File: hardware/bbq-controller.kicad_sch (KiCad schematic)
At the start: 18 parts, among them J1 Barrel_Jack, J2 Probe_Pit, J3 Probe_Meat1, J4 Probe_Meat2, J5 WT32-SC01_Plus, J6 Servo_MG90S, J7 Fan_5015, Q1 IRLZ44N, U1 MP1584EN, U2 ADS1115

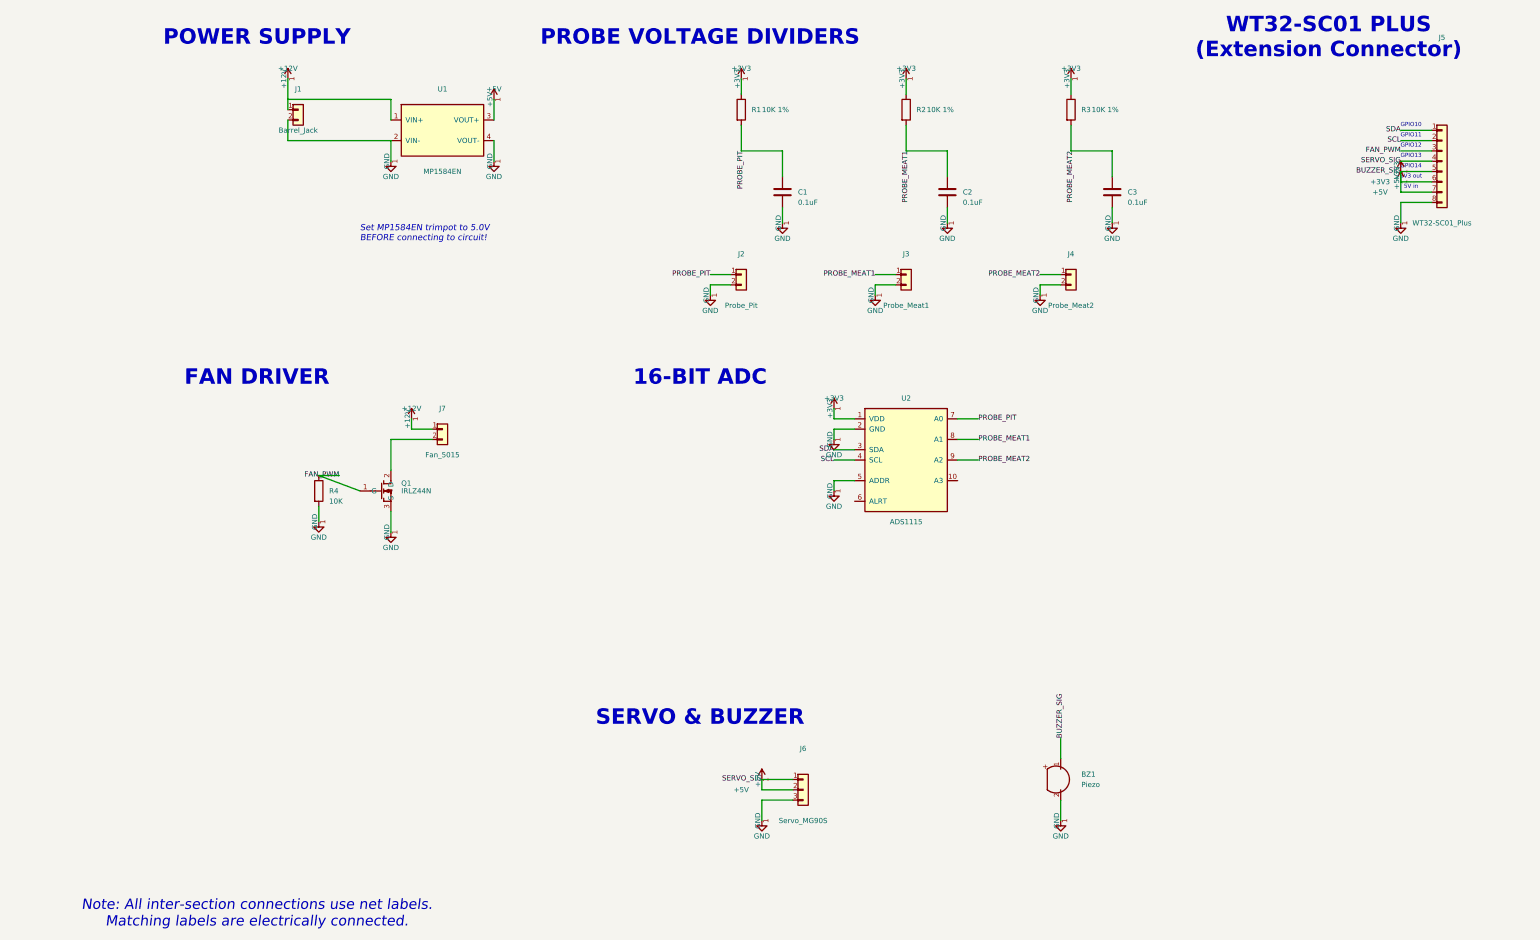
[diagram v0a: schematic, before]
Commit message: Fix KiCad schematic wiring and add perfboard layout to assembly guide
Rewrote the KiCad schematic using a Python generator script that computes
exact pin-to-wire coordinates, fixing all disconnected components. Added a
detailed perfboard layout section to the assembly guide showing component
placement on the 50x70mm board with grid references and back-side wiring
instructions.

Co-Authored-By: Claude Opus 4.6 <noreply@anthropic.com>
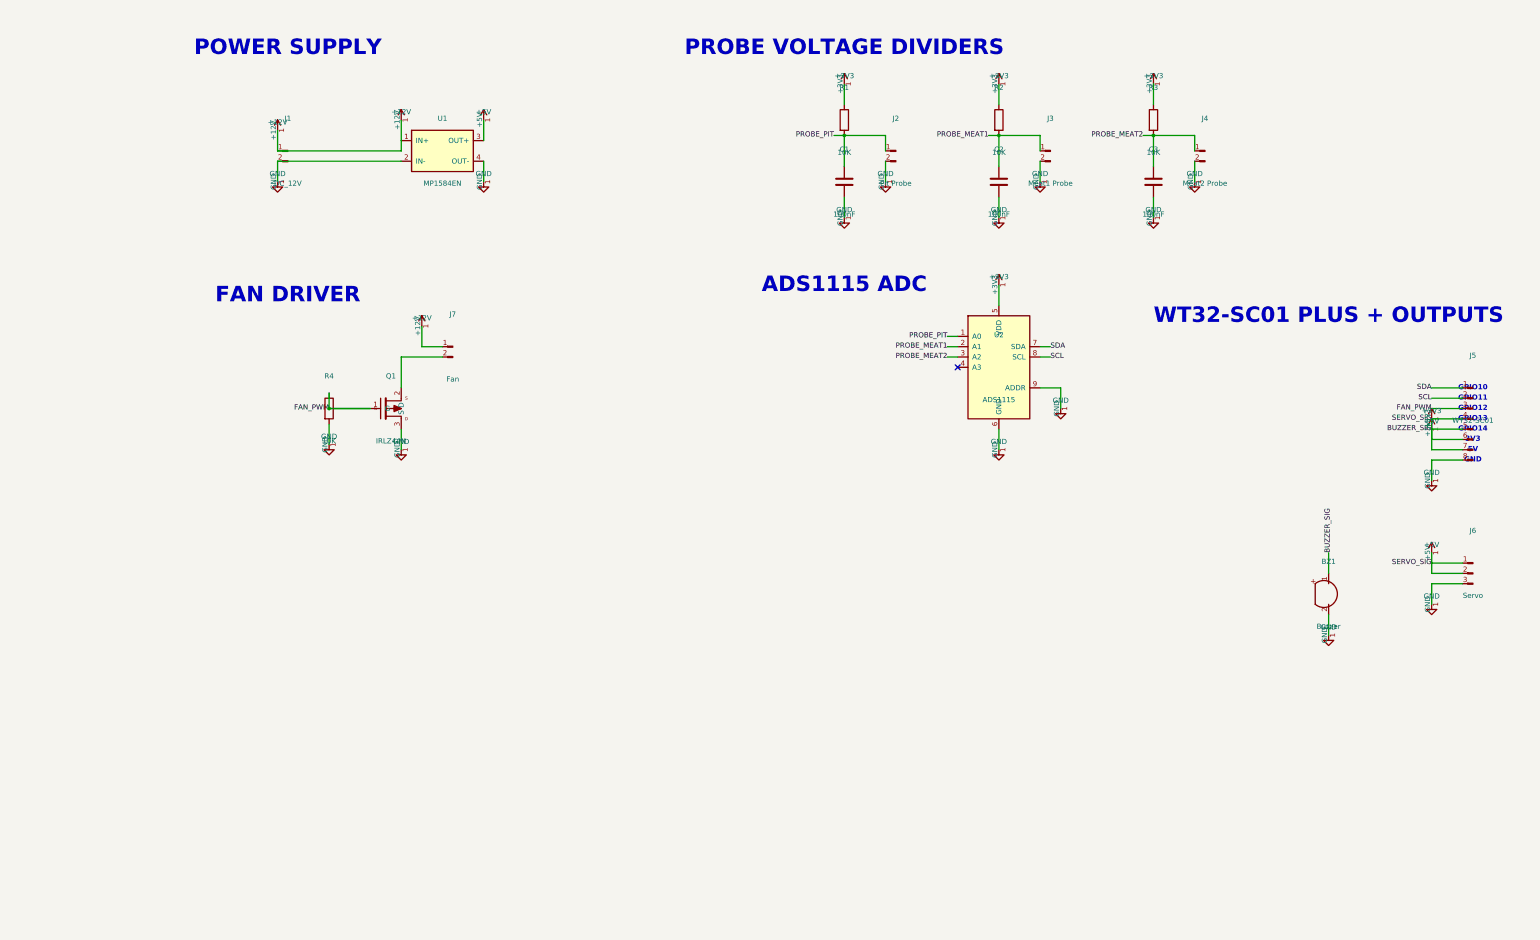
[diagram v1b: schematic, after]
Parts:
- BZ1: value Piezo -> Buzzer
- C1, C2, C3: value 0.1uF -> 100nF
- J1: value Barrel_Jack -> DC_12V
- J2: value Probe_Pit -> Pit Probe
- J3: value Probe_Meat1 -> Meat1 Probe
- J4: value Probe_Meat2 -> Meat2 Probe
- J5: value WT32-SC01_Plus -> WT32-SC01
- J6: value Servo_MG90S -> Servo
- J7: value Fan_5015 -> Fan
- R1, R2, R3: value 10K 1% -> 10K
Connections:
- net +3V3: now also U2.5 (VDD); no longer U2.1 (VDD)
- net GND: now also U2.6 (GND), U2.9 (ADDR); no longer U2.2 (GND), U2.5 (ADDR)
- net PROBE_MEAT1: now also U2.2 (A1); no longer U2.8 (A1)
- net PROBE_MEAT2: now also U2.3 (A2); no longer U2.9 (A2)
- net PROBE_PIT: now also U2.1 (A0); no longer U2.7 (A0)
- net SCL: now also U2.8 (SCL); no longer U2.4 (SCL)
- net SDA: now also U2.7 (SDA); no longer U2.3 (SDA)
- no-connect marks 0 -> 1
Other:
- note added: "3V3"
- note added: "5V"
- note added: "ADS1115 ADC"
- note added: "GND"
- note added: "WT32-SC01 PLUS + OUTPUTS"
- note removed: "16-BIT ADC"
- note removed: "3V3 out"
- note removed: "5V in"
- note removed: "Note: All inter-section connections use net labels. Matching labels are electrically connected."
- note removed: "SERVO & BUZZER"
- note removed: "Set MP1584EN trimpot to 5.0V BEFORE connecting to circuit!"
- note removed: "WT32-SC01 PLUS (Extension Connector)"
